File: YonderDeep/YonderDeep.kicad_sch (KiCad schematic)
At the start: 12 parts, among them J1 GPIO

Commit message: passes jlc gerber viewer
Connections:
- net +3V3: now also J1.17 (Pin_17); no longer J1.1 (Pin_1)
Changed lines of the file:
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@@
   (junction (at 120.65 41.91) (diameter 1.016) (color 0 0 0 0)
   )
-  (junction (at 100.33 24.13) (diameter 0) (color 0 0 0 0)
+  (junction (at 95.25 20.32) (diameter 0) (color 0 0 0 0)
   )
   (junction (at 102.87 78.74) (diameter 0) (color 0 0 0 0)
+  )
+  (junction (at 95.25 24.13) (diameter 0) (color 0 0 0 0)
   )
   (junction (at 102.87 74.93) (diameter 1.016) (color 0 0 0 0)
@@
   (no_connect (at 76.2 69.85))
   (no_connect (at 76.2 49.53))
-  (no_connect (at 100.33 46.99))
   (no_connect (at 144.78 59.69))
   (no_connect (at 203.2 63.5))
@@
   (no_connect (at 243.84 27.94))
   (no_connect (at 203.2 66.04))
+  (no_connect (at 100.33 26.67))
   (no_connect (at 144.78 72.39))
   (no_connect (at 144.78 57.15))
@@
   (no_connect (at 76.2 52.07))
   (no_connect (at 144.78 52.07))
+  (wire (pts (xy 95.25 24.13) (xy 93.98 24.13))
+    (stroke (width 0) (type default) (color 0 0 0 0))
+  )
   (wire (pts (xy 102.87 57.15) (xy 102.87 74.93))
     (stroke (width 0) (type solid) (color 0 0 0 0))
@@
     (stroke (width 0) (type solid) (color 0 0 0 0))
   )
-  (wire (pts (xy 100.33 24.13) (xy 100.33 26.67))
-    (stroke (width 0) (type solid) (color 0 0 0 0))
-  )
   (wire (pts (xy 39.37 120.65) (xy 66.04 120.65))
     (stroke (width 0) (type default) (color 0 0 0 0))
@@
     (stroke (width 0) (type default) (color 0 0 0 0))
   )
-  (wire (pts (xy 100.33 22.86) (xy 100.33 24.13))
-    (stroke (width 0) (type solid) (color 0 0 0 0))
-  )
-  (wire (pts (xy 93.98 24.13) (xy 100.33 24.13))
-    (stroke (width 0) (type default) (color 0 0 0 0))
-  )
   (wire (pts (xy 119.38 125.73) (xy 132.08 125.73))
     (stroke (width 0) (type default) (color 0 0 0 0))
@@
     (stroke (width 0) (type solid) (color 0 0 0 0))
   )
+  (wire (pts (xy 95.25 19.05) (xy 95.25 20.32))
+    (stroke (width 0) (type default) (color 0 0 0 0))
+  )
   (wire (pts (xy 66.04 31.75) (xy 105.41 31.75))
     (stroke (width 0) (type solid) (color 0 0 0 0))
@@
     (stroke (width 0) (type solid) (color 0 0 0 0))
   )
-  (wire (pts (xy 100.33 46.99) (xy 105.41 46.99))
+  (wire (pts (xy 95.25 46.99) (xy 105.41 46.99))
     (stroke (width 0) (type solid) (color 0 0 0 0))
   )
@@
     (stroke (width 0) (type default) (color 0 0 0 0))
   )
+  (wire (pts (xy 95.25 24.13) (xy 95.25 20.32))
+    (stroke (width 0) (type default) (color 0 0 0 0))
+  )
   (wire (pts (xy 120.65 24.13) (xy 128.27 24.13))
     (stroke (width 0) (type default) (color 0 0 0 0))
@@
   )
   (wire (pts (xy 119.38 130.81) (xy 132.08 130.81))
+    (stroke (width 0) (type default) (color 0 0 0 0))
+  )
+  (wire (pts (xy 95.25 46.99) (xy 95.25 24.13))
     (stroke (width 0) (type default) (color 0 0 0 0))
   )
@@
     (pin "1")
   )
-  (symbol (lib_id "power:+3.3V") (at 100.33 22.86 0) (unit 1)
+  (symbol (lib_id "power:+3.3V") (at 95.25 20.32 0) (unit 1)
     (in_bom yes) (on_board yes)
-    (property "Reference" "#PWR04" (id 0) (at 100.33 26.67 0)
+    (property "Reference" "#PWR04" (id 0) (at 95.25 24.13 0)
       (effects (font (size 1.27 1.27)) hide)
     )
-    (property "Value" "+3.3V" (id 1) (at 100.6983 18.5356 0))
-    (property "Footprint" "" (id 2) (at 100.33 22.86 0))
-    (property "Datasheet" "" (id 3) (at 100.33 22.86 0))
+    (property "Value" "+3.3V" (id 1) (at 95.6183 15.9956 0))
+    (property "Footprint" "" (id 2) (at 95.25 20.32 0))
+    (property "Datasheet" "" (id 3) (at 95.25 20.32 0))
     (pin "1")
   )

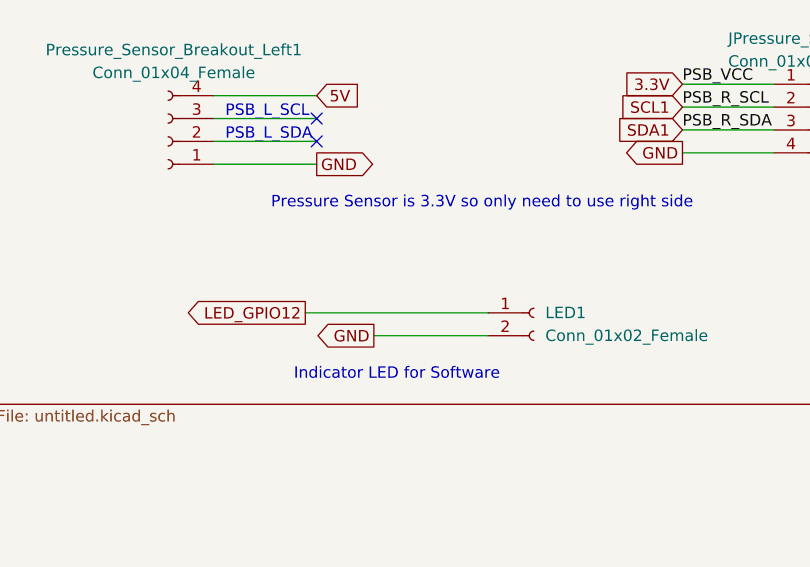
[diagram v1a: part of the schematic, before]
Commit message: LED Resistor added
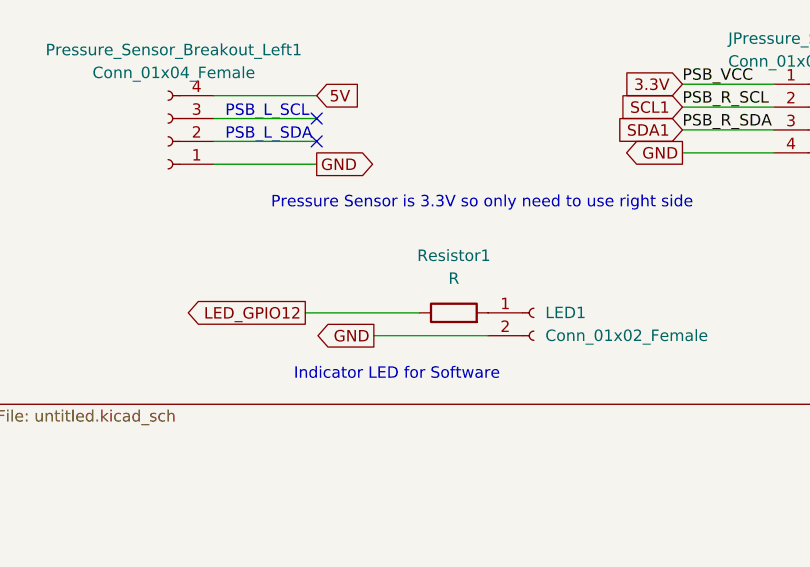
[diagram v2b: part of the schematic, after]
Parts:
- added Resistor1: R, Resistor_THT:R_Box_L8.4mm_W2.5mm_P5.08mm, symbol Device:R
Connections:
- net LED_GPIO12: now also Resistor1.1; no longer LED1.1 (Pin_1)
- new net: LED1.1 (Pin_1), Resistor1.2
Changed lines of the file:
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@@
     (stroke (width 0) (type solid) (color 0 0 0 0))
   )
-  (wire (pts (xy 201.93 85.09) (xy 222.25 85.09))
+  (wire (pts (xy 201.93 85.09) (xy 214.63 85.09))
     (stroke (width 0) (type default) (color 0 0 0 0))
   )
@@
   (wire (pts (xy 102.87 57.15) (xy 105.41 57.15))
     (stroke (width 0) (type solid) (color 0 0 0 0))
+  )
+  (wire (pts (xy 222.25 85.09) (xy 222.25 85.09))
+    (stroke (width 0) (type default) (color 0 0 0 0))
   )
   (wire (pts (xy 118.11 44.45) (xy 144.78 44.45))
@@
     (pin "6")
   )
+  (symbol (lib_id "Device:R") (at 218.44 85.09 90) (unit 1)
+    (in_bom yes) (on_board yes) (fields_autoplaced)
+    (property "Reference" "Resistor1" (id 0) (at 218.44 78.74 90))
+    (property "Value" "R" (id 1) (at 218.44 81.28 90))
+    (property "Footprint" "Resistor_THT:R_Box_L8.4mm_W2.5mm_P5.08mm" (id 2) (at 218.44 86.868 90)
+      (effects (font (size 1.27 1.27)) hide)
+    )
+    (property "Datasheet" "~" (id 3) (at 218.44 85.09 0)
+      (effects (font (size 1.27 1.27)) hide)
+    )
+    (pin "1")
+    (pin "2")
+  )
   (symbol (lib_id "Connector:Conn_01x04_Female") (at 186.69 66.04 180) (unit 1)
     (in_bom yes) (on_board yes) (fields_autoplaced)
@@
       (reference "RIGHT1") (unit 1) (value "Conn_01x02_Female") (footprint "Capacitor_THT:C_Rect_L7.0mm_W2.5mm_P5.00mm")
     )
-  )
+    (path "/a850d2e4-dbd9-4556-80f5-704e652de0db"
+      (reference "Resistor1") (unit 1) (value "R") (footprint "Resistor_THT:R_Box_L8.4mm_W2.5mm_P5.08mm")
+    )
+  )

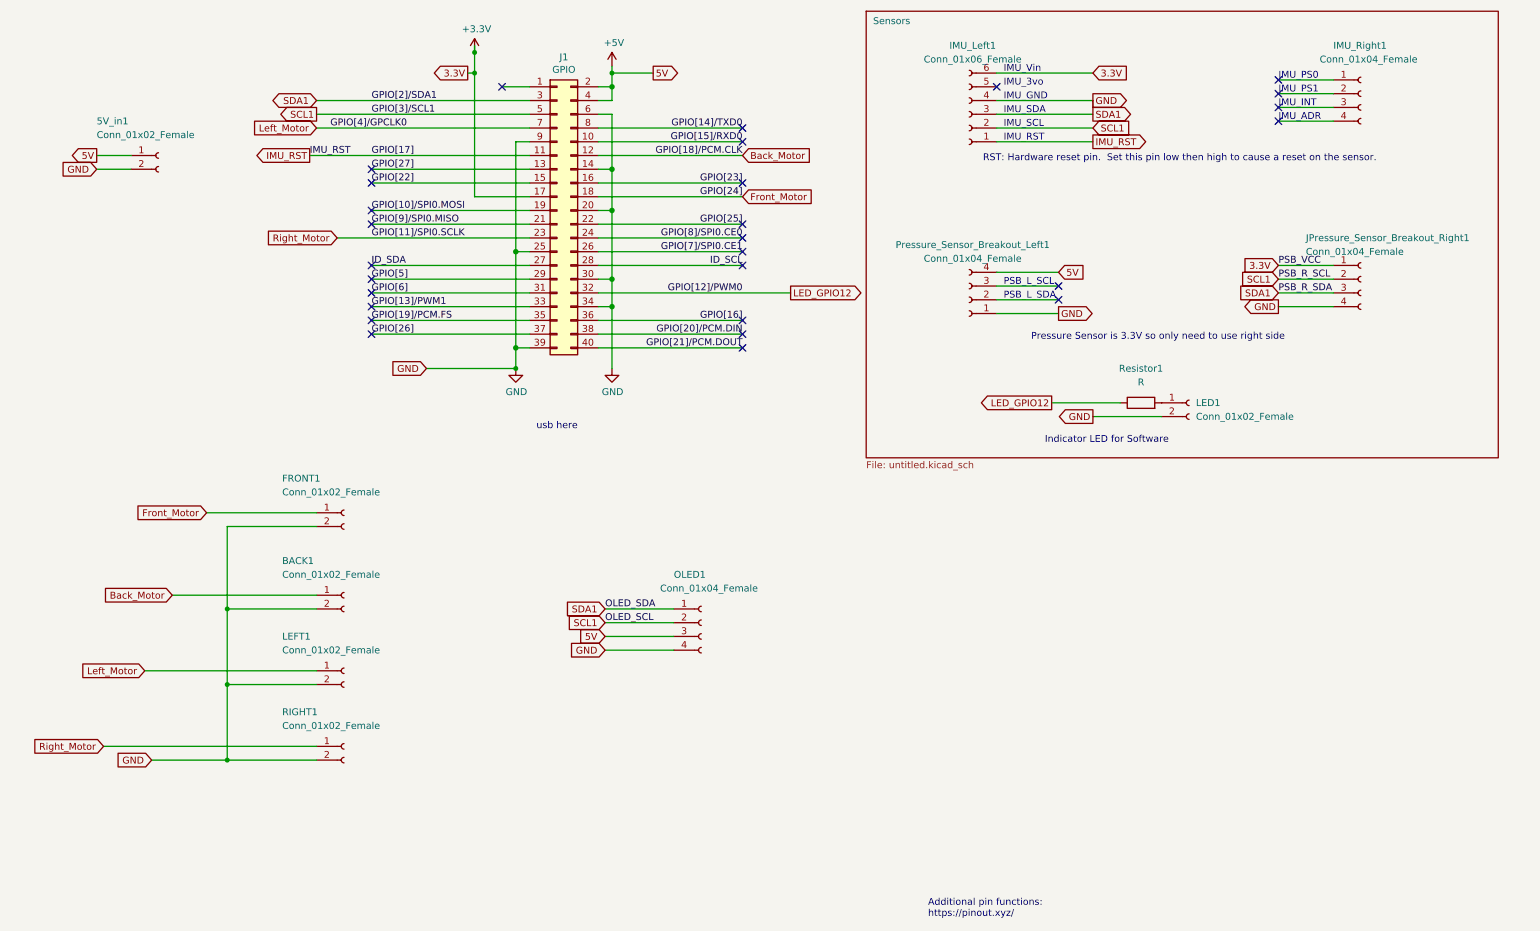
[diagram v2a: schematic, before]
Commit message: Update
PCB update IMU pin footprint and new labels
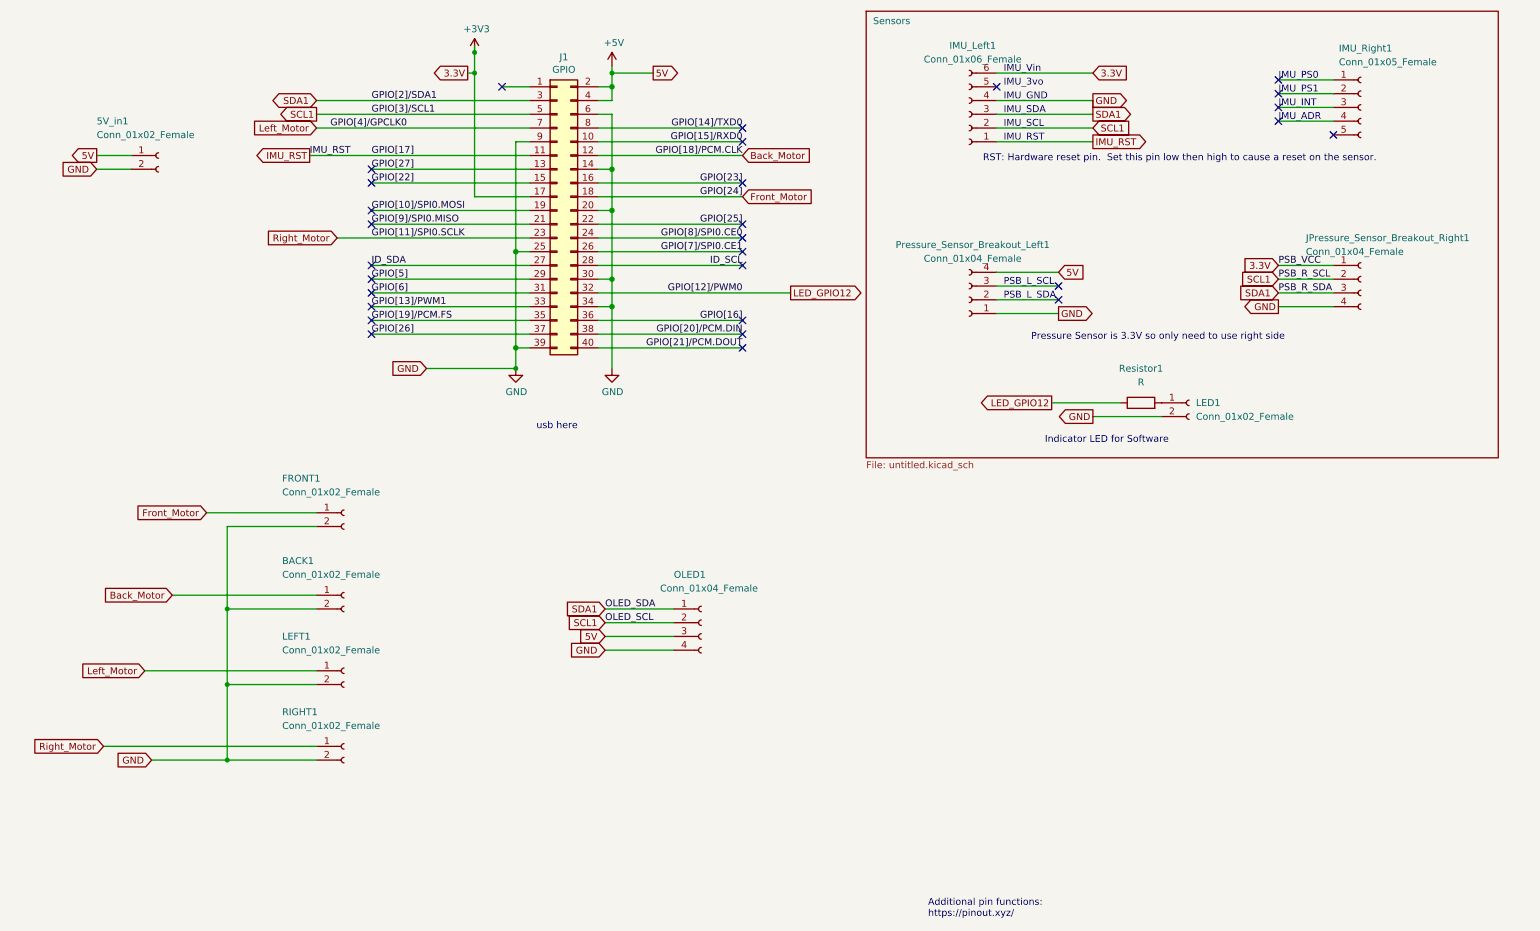
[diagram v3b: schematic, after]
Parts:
- removed IMU_Right1: Conn_01x04_Female, Connector_PinHeader_2.54mm:PinHeader_1x04_P2.54mm_Vertical, symbol Connector:Conn_01x04_Female
- added IMU_Right1: Conn_01x05_Female, Connector_PinHeader_2.54mm:PinHeader_1x05_P2.54mm_Vertical, symbol Connector:Conn_01x05_Socket
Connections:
- no-connect marks 28 -> 29
